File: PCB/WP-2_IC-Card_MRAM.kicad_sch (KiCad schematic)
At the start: 30 parts, among them J1 SMS-138-01-G-S, SW1 CUS-14TB, U1 MRxA08xxYSxxx, U2 MIC5317-3.3YD5, U3 4245, U4 4245, U5 4245, U6 4245

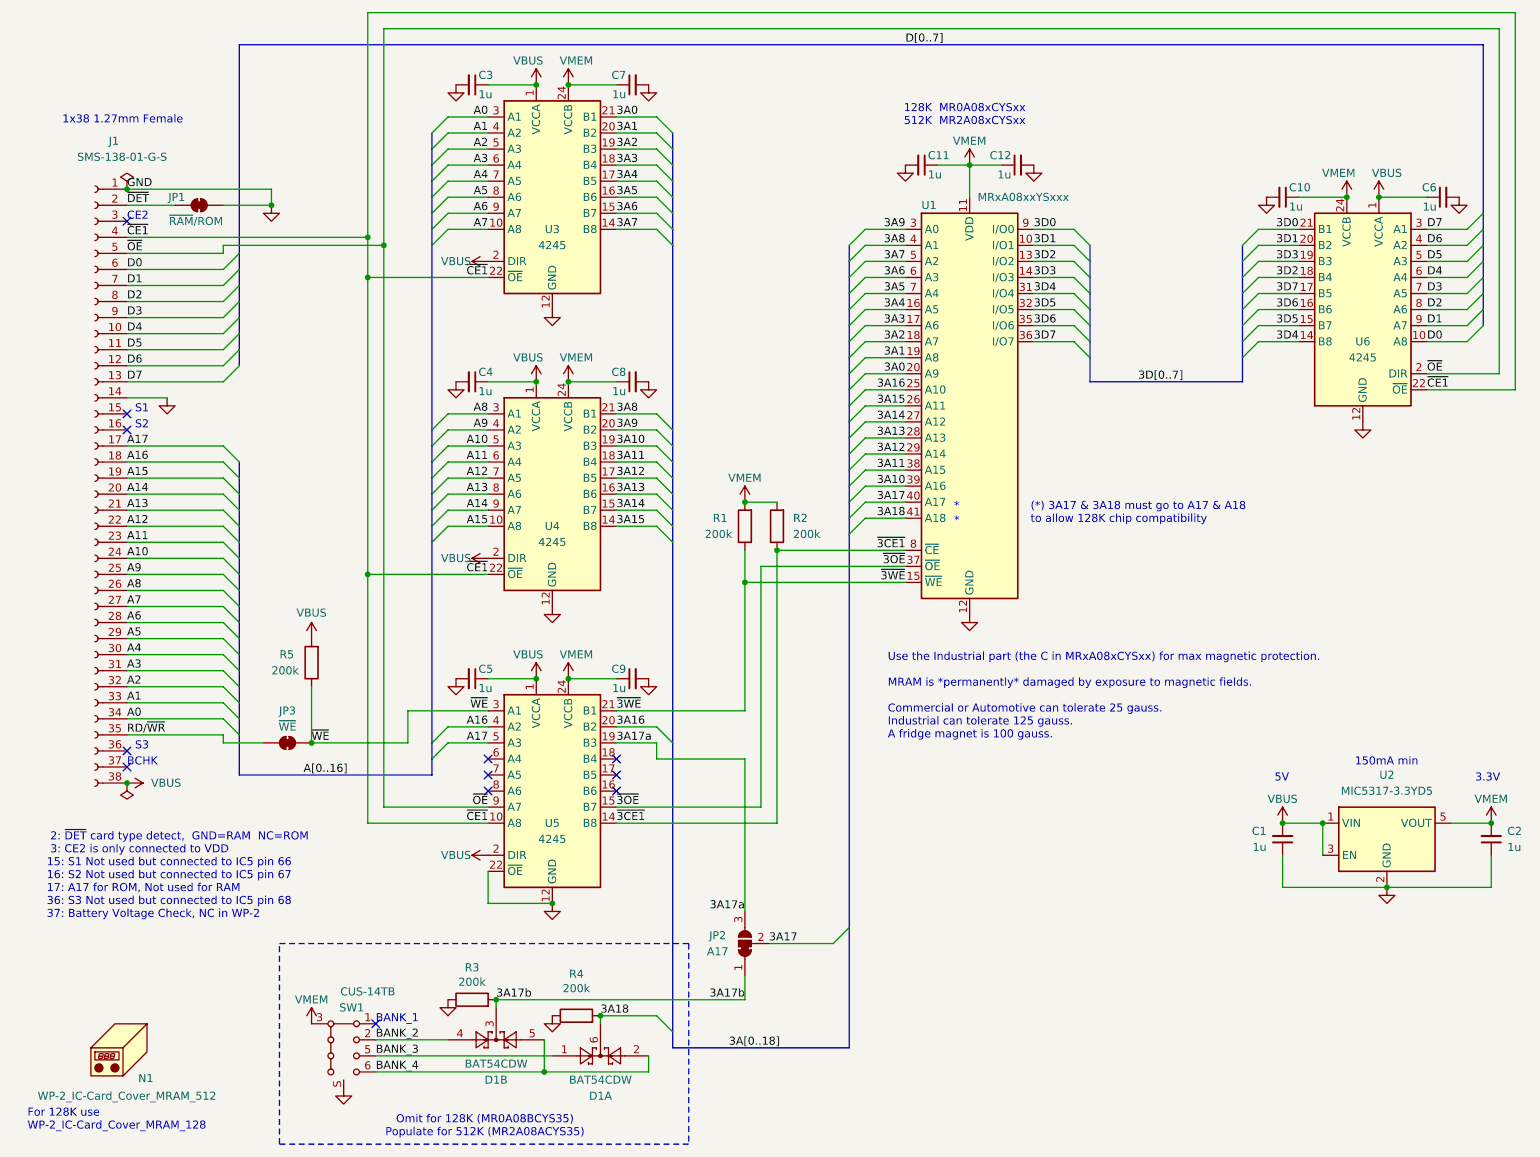
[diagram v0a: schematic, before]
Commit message: new mram pcb touchups, routing /WE, solder jumper pads
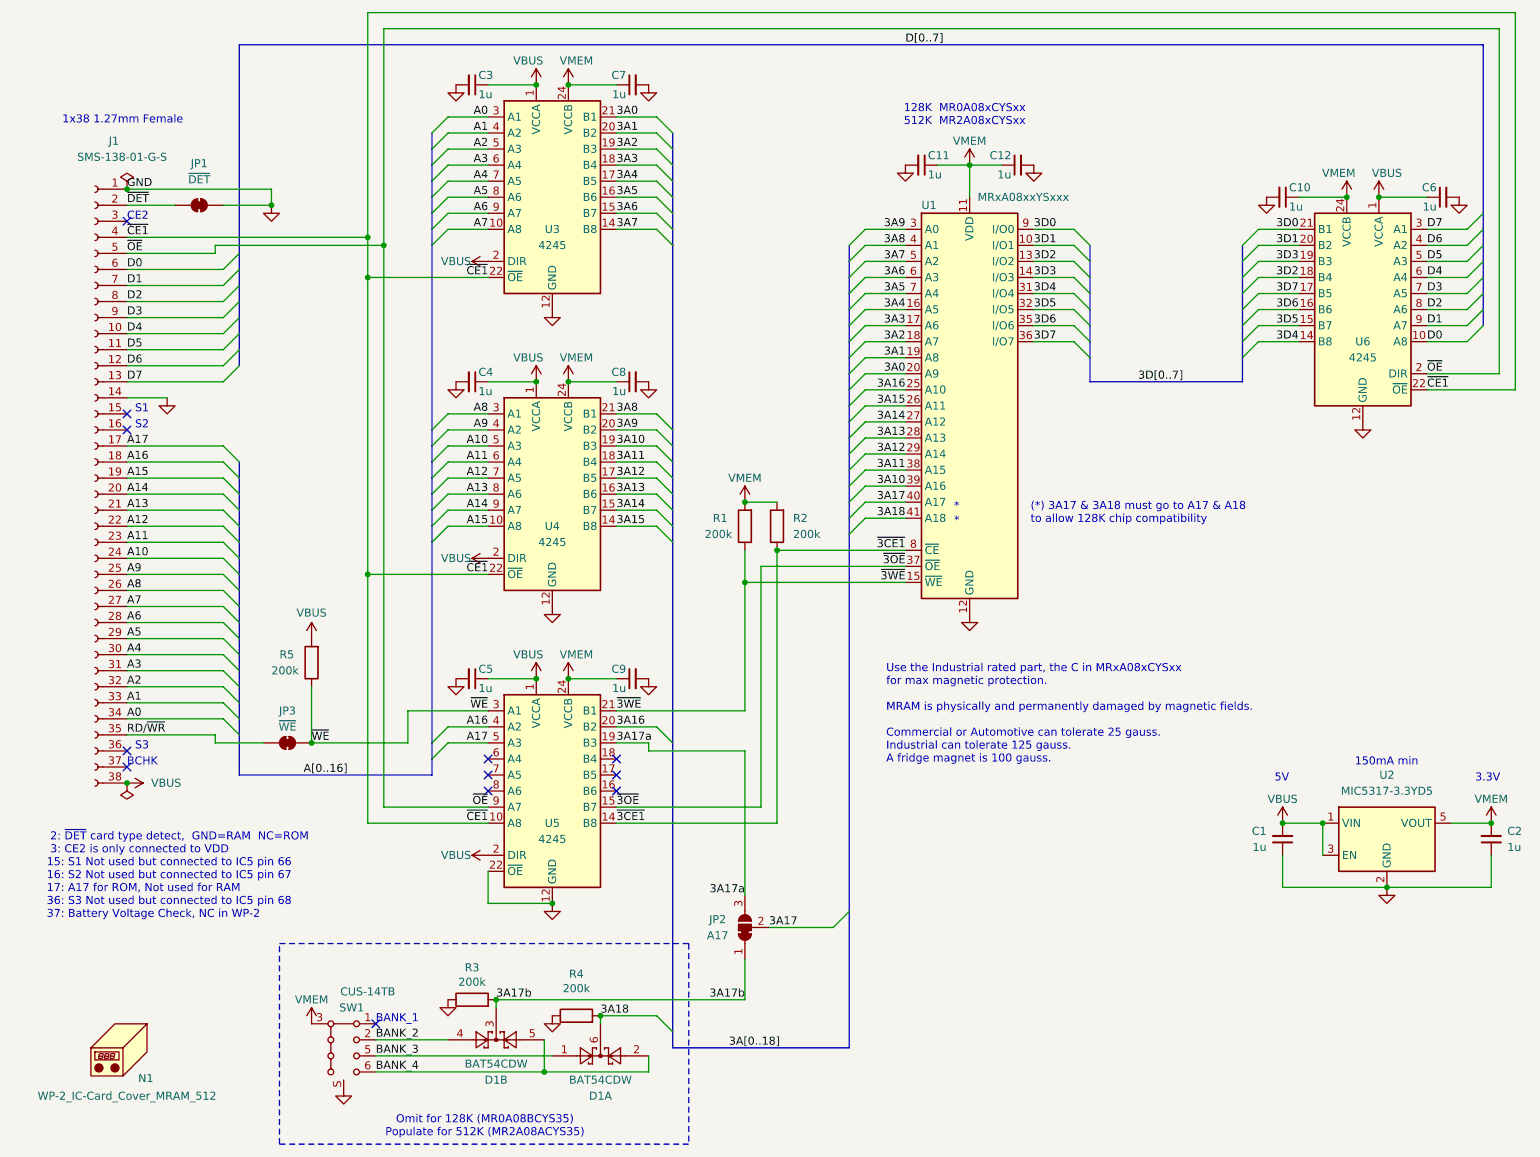
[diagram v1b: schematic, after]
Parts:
- JP1: value ~{RAM}/ROM -> ~{DET}
- SW1: footprint 000_LOCAL:SW_SP4T_CUS-14B pth -> 000_LOCAL:CUS-14TB pth
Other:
- note added: "Use the Industrial rated part, the C in MRxA08xCYSxx for max magnetic protection. MRAM is physically and permanently damaged by magnetic fields. Commercial or Automotive can tolerate 25 gauss. Industrial can tolerate 125 gauss. A fridge magnet is 100 gauss."
- note removed: "For 128K use WP-2_IC-Card_Cover_MRAM_128"
- note removed: "Use the Industrial part (the C in MRxA08xCYSxx) for max magnetic protection. MRAM is *permanently* damaged by exposure to magnetic fields. Commercial or Automotive can tolerate 25 gauss. Industrial can tolerate 125 gauss. A fridge magnet is 100 gauss."
- moved on the sheet: JP2
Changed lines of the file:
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@@
 	)
 	(bus_entry
-		(at 143.51 167.64)
+		(at 143.51 165.1)
 		(size 2.54 -2.54)
 		(stroke
@@
 	(wire
 		(pts
-			(xy 46.99 135.89) (xy 53.34 135.89)
+			(xy 45.72 135.89) (xy 53.34 135.89)
 		)
 		(stroke
@@
 	(wire
 		(pts
-			(xy 129.54 176.53) (xy 129.54 172.72)
+			(xy 129.54 176.53) (xy 129.54 170.18)
 		)
 		(stroke
@@
 	(wire
 		(pts
-			(xy 31.75 58.42) (xy 46.99 58.42)
+			(xy 31.75 58.42) (xy 45.72 58.42)
 		)
 		(stroke
@@
 	(wire
 		(pts
-			(xy 46.99 134.62) (xy 46.99 135.89)
+			(xy 45.72 134.62) (xy 45.72 135.89)
 		)
 		(stroke
@@
 	(wire
 		(pts
-			(xy 115.57 135.89) (xy 109.22 135.89)
+			(xy 114.3 135.89) (xy 109.22 135.89)
 		)
 		(stroke
@@
 	(wire
 		(pts
-			(xy 46.99 57.15) (xy 72.39 57.15)
+			(xy 45.72 57.15) (xy 72.39 57.15)
 		)
 		(stroke
@@
 	(wire
 		(pts
-			(xy 129.54 138.43) (xy 129.54 162.56)
+			(xy 129.54 137.16) (xy 129.54 160.02)
 		)
 		(stroke
@@
 	(wire
 		(pts
-			(xy 46.99 57.15) (xy 46.99 58.42)
+			(xy 45.72 57.15) (xy 45.72 58.42)
 		)
 		(stroke
@@
 	(bus
 		(pts
-			(xy 146.05 102.87) (xy 146.05 165.1)
+			(xy 146.05 102.87) (xy 146.05 162.56)
 		)
 		(stroke
@@
 	(wire
 		(pts
-			(xy 129.54 138.43) (xy 115.57 138.43)
+			(xy 129.54 137.16) (xy 114.3 137.16)
 		)
 		(stroke
@@
 	(wire
 		(pts
-			(xy 133.35 167.64) (xy 143.51 167.64)
+			(xy 133.35 165.1) (xy 143.51 165.1)
 		)
 		(stroke
@@
 	(wire
 		(pts
-			(xy 115.57 138.43) (xy 115.57 135.89)
+			(xy 114.3 137.16) (xy 114.3 135.89)
 		)
 		(stroke
@@
 	(wire
 		(pts
-			(xy 46.99 134.62) (xy 31.75 134.62)
+			(xy 45.72 134.62) (xy 31.75 134.62)
 		)
 		(stroke
@@
 	(bus
 		(pts
-			(xy 146.05 165.1) (xy 146.05 184.15)
+			(xy 146.05 162.56) (xy 146.05 184.15)
 		)
 		(stroke
@@
 		)
 	)
-	(text "Use the Industrial part (the C in MRxA08xCYSxx) for max magnetic protection.\n\nMRAM is *permanently* damaged by exposure to magnetic fields.\n\nCommercial or Automotive can tolerate 25 gauss.\nIndustrial can tolerate 125 gauss.\nA fridge magnet is 100 gauss.\n"
+	(text "Use the Industrial rated part, the C in MRxA08xCYSxx\nfor max magnetic protection.\n\nMRAM is physically and permanently damaged by magnetic fields.\n\nCommercial or Automotive can tolerate 25 gauss.\nIndustrial can tolerate 125 gauss.\nA fridge magnet is 100 gauss.\n"
 		(exclude_from_sim no)
-		(at 152.146 121.666 0)
+		(at 151.892 123.444 0)
 		(effects
 			(font
@@
 		)
 	)
-	(text "For 128K use\nWP-2_IC-Card_Cover_MRAM_128"
-		(exclude_from_sim no)
-		(at 16.002 193.802 0)
-		(effects
-			(font
-				(size 1.27 1.27)
-			)
-			(justify left top)
-		)
-	)
 	(text "1x38 1.27mm Female"
 		(exclude_from_sim no)
@@
 	)
 	(label "3A17a"
-		(at 129.54 162.56 180)
+		(at 129.54 160.02 180)
 		(fields_autoplaced yes)
 		(effects
@@
 	)
 	(label "3A17"
-		(at 133.35 167.64 0)
+		(at 133.35 165.1 0)
 		(fields_autoplaced yes)
 		(effects
@@
 	(symbol
 		(lib_id "000_LOCAL:SolderJumper_3_Bridged12")
-		(at 129.54 167.64 90)
+		(at 129.54 165.1 90)
 		(unit 1)
 		(exclude_from_sim yes)
@@
 		(dnp no)
 		(property "Reference" "JP2"
-			(at 125.222 166.37 90)
+			(at 125.222 163.83 90)
 			(effects
 				(font
@@
 		)
 		(property "Value" "A17"
-			(at 125.222 168.91 90)
+			(at 125.222 166.37 90)
 			(effects
 				(font
@@
 		)
 		(property "Footprint" "000_LOCAL:SolderJumper-3_P1.3mm_Bridged12_RoundedPad1.0x1.5mm"
-			(at 129.54 167.64 0)
+			(at 129.54 165.1 0)
 			(effects
 				(font
@@
 		)
 		(property "Datasheet" "~"
-			(at 129.54 167.64 0)
+			(at 129.54 165.1 0)
 			(effects
 				(font
@@
 		)
 		(property "Description" "3-pole Solder Jumper, pins 1+2 closed/bridged"
-			(at 129.54 167.64 0)
+			(at 129.54 165.1 0)
 			(effects
 				(font
@@
 		(dnp no)
 		(property "Reference" "JP1"
-			(at 39.624 49.53 0)
+			(at 43.18 44.196 0)
 			(effects
 				(font
@@
 			)
 		)
-		(property "Value" "~{RAM}/ROM"
-			(at 42.672 53.34 0)
+		(property "Value" "~{DET}"
+			(at 43.18 46.736 0)
 			(effects
 				(font
@@
 			)
 		)
-		(property "Footprint" "000_LOCAL:SW_SP4T_CUS-14B pth"
+		(property "Footprint" "000_LOCAL:CUS-14TB pth"
 			(at 50.165 179.705 0)
 			(effects

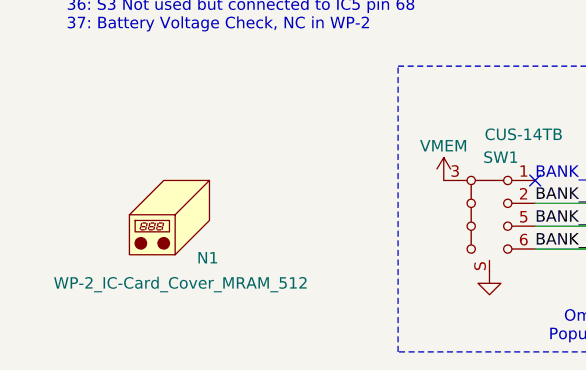
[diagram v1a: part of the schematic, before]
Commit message: update covers for flash & mram with bank sw & write sw
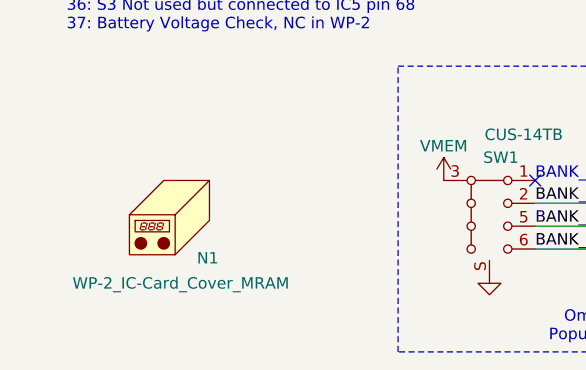
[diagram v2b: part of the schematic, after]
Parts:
- N1: value WP-2_IC-Card_Cover_MRAM_512 -> WP-2_IC-Card_Cover_MRAM; footprint 000_LOCAL:WP-2_IC-Card_Cover_MRAM_512 -> 000_LOCAL:WP-2_IC-Card_Cover_MRAM
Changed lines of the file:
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@@
 			)
 		)
-		(property "Value" "WP-2_IC-Card_Cover_MRAM_512"
+		(property "Value" "WP-2_IC-Card_Cover_MRAM"
 			(at 31.75 191.77 0)
 			(effects
@@
 			)
 		)
-		(property "Footprint" "000_LOCAL:WP-2_IC-Card_Cover_MRAM_512"
+		(property "Footprint" "000_LOCAL:WP-2_IC-Card_Cover_MRAM"
 			(at 33.02 182.88 0)
 			(effects

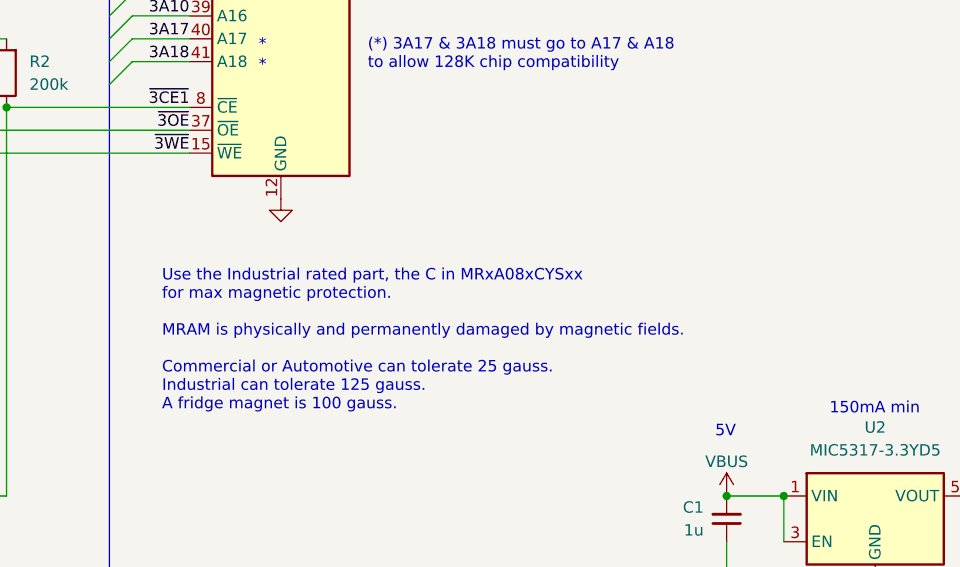
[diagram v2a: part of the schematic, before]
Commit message: mram routing & silkscreen polish
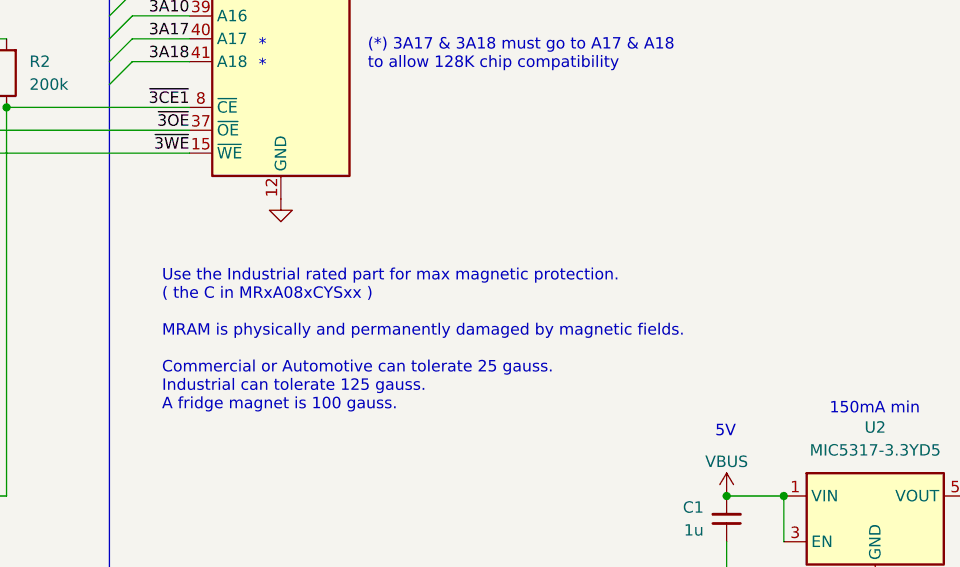
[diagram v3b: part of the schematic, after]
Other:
- note added: "Use the Industrial rated part for max magnetic protection. ( the C in MRxA08xCYSxx ) MRAM is physically and permanently damaged by magnetic fields. Commercial or Automotive can tolerate 25 gauss. Industrial can tolerate 125 gauss. A fridge magnet is 100 gauss."
- note removed: "Use the Industrial rated part, the C in MRxA08xCYSxx for max magnetic protection. MRAM is physically and permanently damaged by magnetic fields. Commercial or Automotive can tolerate 25 gauss. Industrial can tolerate 125 gauss. A fridge magnet is 100 gauss."
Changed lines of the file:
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@@
 		)
 	)
-	(text "Use the Industrial rated part, the C in MRxA08xCYSxx\nfor max magnetic protection.\n\nMRAM is physically and permanently damaged by magnetic fields.\n\nCommercial or Automotive can tolerate 25 gauss.\nIndustrial can tolerate 125 gauss.\nA fridge magnet is 100 gauss.\n"
+	(text "Use the Industrial rated part for max magnetic protection.\n( the C in MRxA08xCYSxx )\n\nMRAM is physically and permanently damaged by magnetic fields.\n\nCommercial or Automotive can tolerate 25 gauss.\nIndustrial can tolerate 125 gauss.\nA fridge magnet is 100 gauss.\n"
 		(exclude_from_sim no)
 		(at 151.892 123.444 0)
